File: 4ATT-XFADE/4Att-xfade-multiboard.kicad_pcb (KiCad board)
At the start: 2 copper layers, 158.3 x 82.2 mm, 39 parts, among them J1 IN1, J2 IN2, J3 IN3, J4 IN4, J5 OUT1, J6 OUT2, J7 OUT3, J8 OUT4, J9 MIX, SW1 Mute3, SW2 Mute4, SW3 Mute1, SW4 Mute2, SW5 LIN/LOG, SW6 Mute

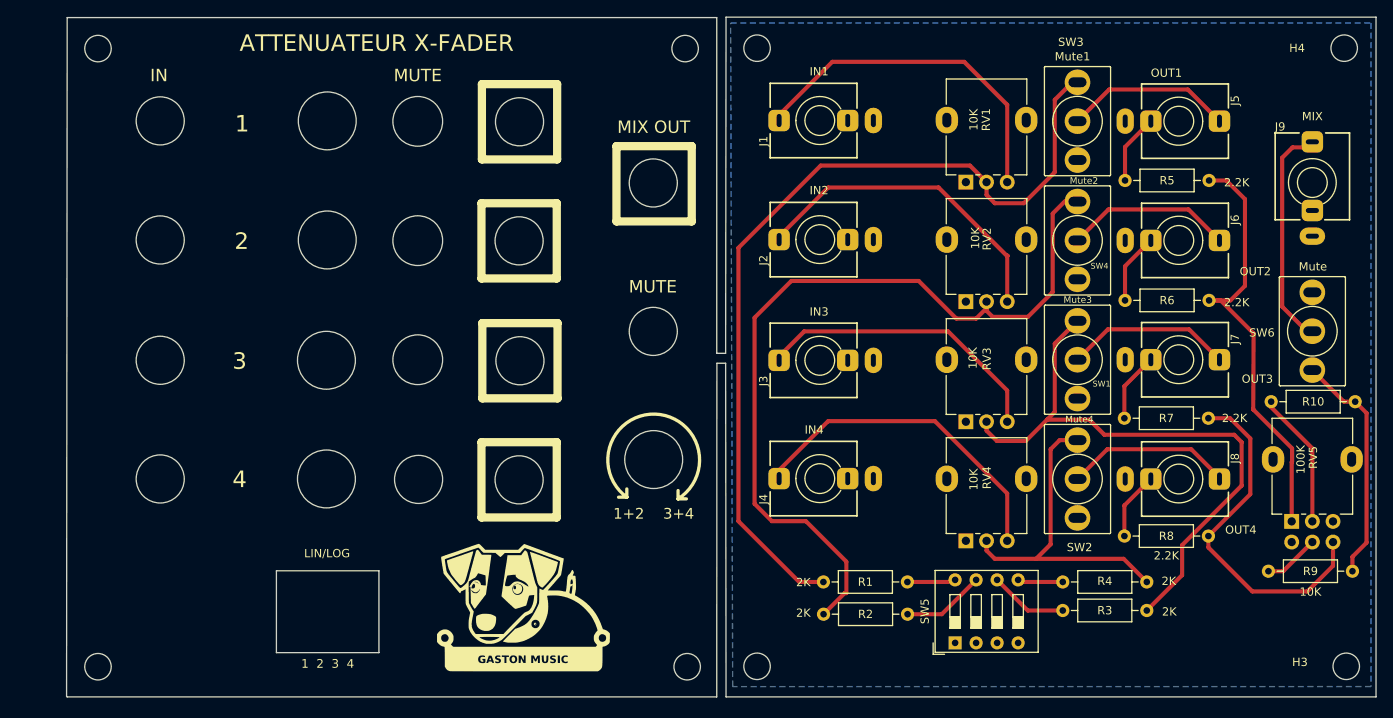
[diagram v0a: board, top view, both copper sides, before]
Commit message: correction Mute
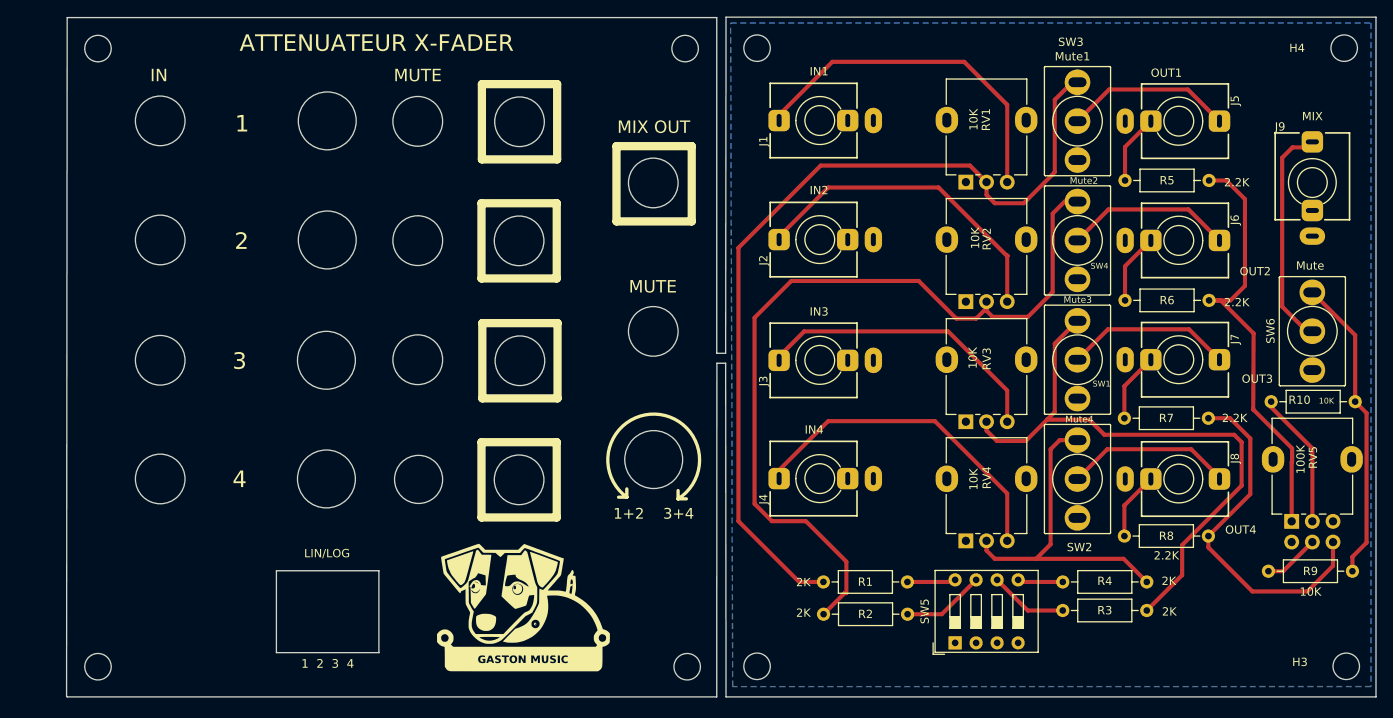
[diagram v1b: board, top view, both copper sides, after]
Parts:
- turned SW6 to 180 degrees
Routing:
- net Net-(R10-Pad1): track 28.5 -> 37.1 mm
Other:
- outline, holes or cut-outs redrawn
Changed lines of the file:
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@@
   (net 26 "Net-(R3-Pad1)")
   (net 27 "Net-(R4-Pad1)")
-  (net 28 "Net-(RV5-Pad1)")
+  (net 28 "Net-(R5-Pad2)")
   (net 29 "Net-(R7-Pad2)")
   (net 30 "Net-(R10-Pad1)")
@@
       (net 9 "norm1") (pintype "passive"))
     (pad "2" thru_hole oval (at 10.16 0) (size 1.6 1.6) (drill 0.8) (layers *.Cu *.Mask)
-      (net 28 "Net-(RV5-Pad1)") (pintype "passive"))
+      (net 28 "Net-(R5-Pad2)") (pintype "passive"))
     (model "${KICAD6_3DMODEL_DIR}/Resistor_THT.3dshapes/R_Axial_DIN0207_L6.3mm_D2.5mm_P10.16mm_Horizontal.wrl"
       (offset (xyz 0 0 0))
@@
     (pad "" thru_hole oval (at 7.5 -2.25 180) (size 2.72 3.24) (drill oval 1.1 1.8) (layers *.Cu *.Mask))
     (pad "1" thru_hole rect (at 0 0 180) (size 1.8 1.8) (drill 1) (layers *.Cu *.Mask)
-      (net 28 "Net-(RV5-Pad1)") (pinfunction "1") (pintype "passive"))
+      (net 28 "Net-(R5-Pad2)") (pinfunction "1") (pintype "passive"))
     (pad "2" thru_hole circle (at 0 2.5 180) (size 1.8 1.8) (drill 1) (layers *.Cu *.Mask)
       (net 32 "Net-(R10-Pad2)") (pinfunction "2") (pintype "passive"))
@@
   )
   (footprint "4MS_switch:Switch_Toggle_SPDT_Mini_SolderLug" (layer "F.Cu")
-    (at 176.65 80.7275)
+    (at 176.65 80.7275 180)
     (property "Sheetfile" "4Att-xfade-multiboard.kicad_sch")
     (property "Sheetname" "")
     (attr through_hole)
-    (fp_text reference "SW6" (at -7.65 0.7725) (layer "F.SilkS")
-      (effects (font (size 1 1) (thickness 0.15)) (justify left bottom))
+    (fp_text reference "SW6" (at 4.45 1.5775 90) (layer "F.SilkS")
+      (effects (font (size 1 1) (thickness 0.15)) (justify right bottom))
     )
-    (fp_text value "Mute" (at -1.65 -7.2275) (layer "F.SilkS")
-      (effects (font (size 1 1) (thickness 0.15)) (justify left bottom))
+    (fp_text value "Mute" (at -1.45 7.3275) (layer "F.SilkS")
+      (effects (font (size 1 1) (thickness 0.15)) (justify right bottom))
     )
     (fp_line (start 3.9 6.6) (end -3.9 6.6) (layer "F.SilkS") (width 0.125))
@@
     (fp_line (start -3.9 6.5) (end -3.9 -6.5) (layer "F.CrtYd") (width 0.05))
     (fp_line (start 3.9 6.5) (end -3.9 6.5) (layer "F.CrtYd") (width 0.05))
-    (pad "1" thru_hole circle locked (at 0 -4.7) (size 3.1 3.1) (drill oval 2.2 1.2) (layers *.Cu *.Mask)
+    (pad "1" thru_hole circle locked (at 0 -4.7 180) (size 3.1 3.1) (drill oval 2.2 1.2) (layers *.Cu *.Mask)
       (net 25 "GND") (pinfunction "A") (pintype "passive"))
-    (pad "2" thru_hole circle locked (at 0 0) (size 3.1 3.1) (drill oval 2.2 1.2) (layers *.Cu *.Mask)
+    (pad "2" thru_hole circle locked (at 0 0 180) (size 3.1 3.1) (drill oval 2.2 1.2) (layers *.Cu *.Mask)
       (net 17 "Net-(J9-PadT)") (pinfunction "B") (pintype "passive"))
-    (pad "3" thru_hole circle locked (at 0 4.7) (size 3.1 3.1) (drill oval 2.2 1.2) (layers *.Cu *.Mask)
+    (pad "3" thru_hole circle locked (at 0 4.7 180) (size 3.1 3.1) (drill oval 2.2 1.2) (layers *.Cu *.Mask)
       (net 30 "Net-(R10-Pad1)") (pinfunction "C") (pintype "passive"))
     (model "/Users/design/Google Drive/4ms/kicad/packages3d/spdt-toggle-submini.wrl"
@@
     (property "Sheetname" "")
     (attr through_hole)
-    (fp_text reference "R10" (at 5.08 0) (layer "F.SilkS")
+    (fp_text reference "R10" (at 6.73 0.2) (layer "F.SilkS")
       (effects (font (size 1 1) (thickness 0.15)))
     )
-    (fp_text value "10K" (at 5.08 2.37) (layer "F.Fab")
-      (effects (font (size 1 1) (thickness 0.15)))
+    (fp_text value "10K" (at 3.48 0.1) (layer "F.SilkS")
+      (effects (font (size 0.7 0.7) (thickness 0.15)))
     )
     (fp_text user "${REFERENCE}" (at 5.08 0) (layer "F.Fab")
@@
       (net 10 "norm2") (pintype "passive"))
     (pad "2" thru_hole oval (at 10.16 0) (size 1.6 1.6) (drill 0.8) (layers *.Cu *.Mask)
-      (net 28 "Net-(RV5-Pad1)") (pintype "passive"))
+      (net 28 "Net-(R5-Pad2)") (pintype "passive"))
     (model "${KICAD6_3DMODEL_DIR}/Resistor_THT.3dshapes/R_Axial_DIN0207_L6.3mm_D2.5mm_P10.16mm_Horizontal.wrl"
       (offset (xyz 0 0 0))
@@
   (gr_line locked (start 92.750001 100.8) (end 93.750001 100.799999) (layer "F.SilkS") (width 0.4))
   (gr_line locked (start 99.95 100) (end 99.950001 101) (layer "F.SilkS") (width 0.4))
-  (gr_circle locked (center 37.325001 55.293112) (end 39.225001 57.493112) (layer "Edge.Cuts") (width 0.1) (fill none))
-  (gr_circle locked (center 37.325001 69.693112) (end 39.225001 71.893112) (layer "Edge.Cuts") (width 0.1) (fill none))
+  (gr_circle locked (center 37.325001 55.293112) (end 40.325001 55.293112) (layer "Edge.Cuts") (width 0.1) (fill none))
+  (gr_circle locked (center 37.325001 69.693112) (end 40.325001 69.693112) (layer "Edge.Cuts") (width 0.1) (fill none))
   (gr_circle locked (center 68.468113 55.35) (end 70.518113 57.55) (layer "Edge.Cuts") (width 0.1) (fill none))
   (gr_circle locked (center 57.425001 84.243112) (end 59.525001 87.043112) (layer "Edge.Cuts") (width 0.1) (fill none))
   (gr_circle locked (center 57.525001 55.293112) (end 59.625001 58.093112) (layer "Edge.Cuts") (width 0.1) (fill none))
-  (gr_circle locked (center 80.825001 84.3) (end 82.725001 86.5) (layer "Edge.Cuts") (width 0.1) (fill none))
-  (gr_circle locked (center 80.775001 55.4) (end 82.675001 57.6) (layer "Edge.Cuts") (width 0.1) (fill none))
+  (gr_circle locked (center 80.825001 84.3) (end 83.825001 84.3) (layer "Edge.Cuts") (width 0.1) (fill none))
+  (gr_circle locked (center 80.775001 55.4) (end 83.775001 55.4) (layer "Edge.Cuts") (width 0.1) (fill none))
   (gr_poly
     (pts
@@
   (gr_circle locked (center 68.468113 69.775) (end 70.518113 71.975) (layer "Edge.Cuts") (width 0.1) (fill none))
   (gr_circle locked (center 68.468113 84.175) (end 70.518113 86.375) (layer "Edge.Cuts") (width 0.1) (fill none))
-  (gr_circle locked (center 37.325001 98.593112) (end 39.225001 100.793112) (layer "Edge.Cuts") (width 0.1) (fill none))
-  (gr_circle locked (center 80.725001 98.7) (end 82.625001 100.9) (layer "Edge.Cuts") (width 0.1) (fill none))
-  (gr_circle locked (center 37.325001 84.243112) (end 39.225001 86.443112) (layer "Edge.Cuts") (width 0.1) (fill none))
+  (gr_circle locked (center 37.325001 98.593112) (end 40.325001 98.593112) (layer "Edge.Cuts") (width 0.1) (fill none))
+  (gr_circle locked (center 80.725001 98.7) (end 83.725001 98.7) (layer "Edge.Cuts") (width 0.1) (fill none))
+  (gr_circle locked (center 37.325001 84.243112) (end 40.325001 84.243112) (layer "Edge.Cuts") (width 0.1) (fill none))
   (gr_rect locked (start 51.375001 109.7) (end 63.775001 119.6) (layer "Edge.Cuts") (width 0.1) (fill none))
-  (gr_circle locked (center 96.950001 80.75) (end 98.850001 82.95) (layer "Edge.Cuts") (width 0.1) (fill none))
+  (gr_circle locked (center 96.950001 80.75) (end 99.950001 80.75) (layer "Edge.Cuts") (width 0.1) (fill none))
   (gr_circle locked (center 57.425001 98.593112) (end 59.525001 101.393112) (layer "Edge.Cuts") (width 0.1) (fill none))
-  (gr_circle locked (center 80.725001 69.8) (end 82.625001 72) (layer "Edge.Cuts") (width 0.1) (fill none))
-  (gr_circle locked (center 96.950001 62.8) (end 98.850001 65) (layer "Edge.Cuts") (width 0.1) (fill none))
+  (gr_circle locked (center 80.725001 69.8) (end 83.725001 69.8) (layer "Edge.Cuts") (width 0.1) (fill none))
+  (gr_circle locked (center 96.950001 62.8) (end 99.950001 62.8) (layer "Edge.Cuts") (width 0.1) (fill none))
   (gr_text "JLCJLCJLCJLC" (at 41.925001 120.0425) (layer "B.SilkS")
     (effects (font (size 1 1) (thickness 0.15)))
@@
   (segment (start 169.15 93.7) (end 169.15 100.43) (width 0.5) (layer "F.Cu") (net 29))
   (segment (start 164.08 91.25) (end 166.7 91.25) (width 0.5) (layer "F.Cu") (net 29))
-  (segment (start 181.83 89.25) (end 180.4725 89.25) (width 0.5) (layer "F.Cu") (net 30))
-  (segment (start 180.4725 89.25) (end 176.65 85.4275) (width 0.5) (layer "F.Cu") (net 30))
+  (segment (start 181.83 89.25) (end 181.83 81.2075) (width 0.5) (layer "F.Cu") (net 30))
   (segment (start 181.5 108) (end 183.21 106.29) (width 0.5) (layer "F.Cu") (net 30))
   (segment (start 181.5 109.75) (end 181.5 108) (width 0.5) (layer "F.Cu") (net 30))
+  (segment (start 181.83 81.2075) (end 176.65 76.0275) (width 0.5) (layer "F.Cu") (net 30))
   (segment (start 183.21 90.63) (end 181.83 89.25) (width 0.5) (layer "F.Cu") (net 30))
   (segment (start 183.21 106.29) (end 183.21 90.63) (width 0.5) (layer "F.Cu") (net 30))

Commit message: ajout image
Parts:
- moved REF** 5.93 mm to (23.9, 121.6)
- moved REF** 5.93 mm to (23.9, 46.9)
- moved G*** 5.93 mm to (75.3, 116.6)
- moved REF** 5.93 mm to (94.9, 46.9)
- moved REF** 5.93 mm to (95.1, 121.6)
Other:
- board size 158.3 x 82.2 mm -> 164.3 x 82.7 mm
